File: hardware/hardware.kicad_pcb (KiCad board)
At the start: 2 copper layers, 45 x 45 mm, 27 parts, among them J2 USB_B_Micro, J3 Conn_01x05_Pin, U1 CH32V003F4P6, U3 AMS1117-3.3

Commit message: fix button
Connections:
- U1 pad 16: unconnected-(U1-PC6/MOSI-Pad16) -> BUTTON
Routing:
- net BUTTON: track 114.3 -> 134.1 mm, vias 0 -> 2

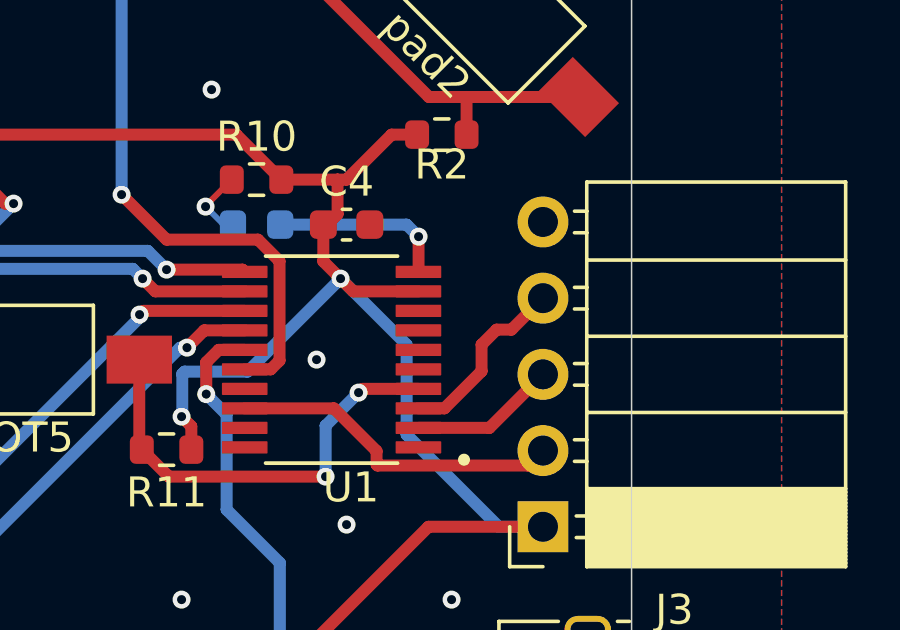
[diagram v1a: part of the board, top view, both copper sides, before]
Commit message: fix mcu ground issue
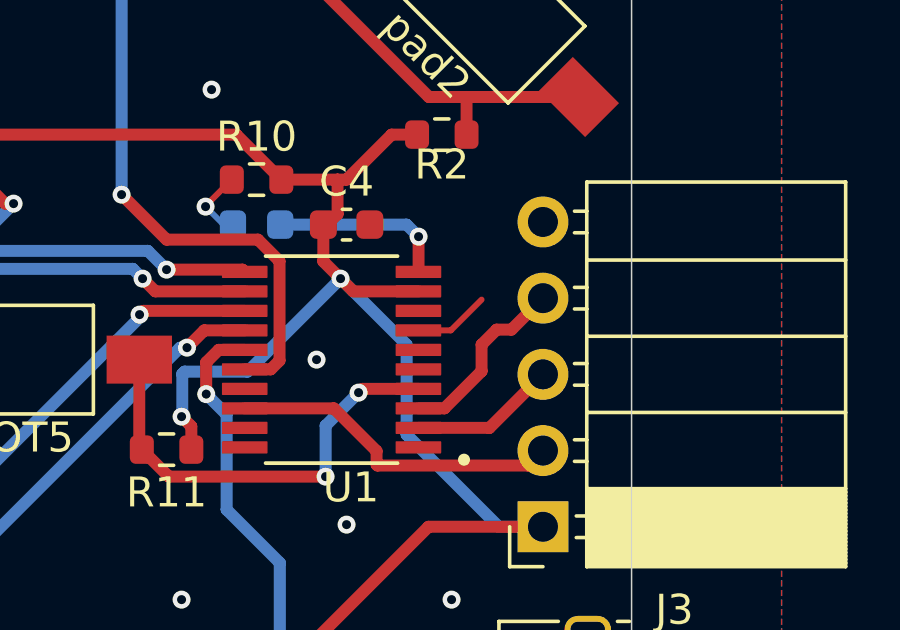
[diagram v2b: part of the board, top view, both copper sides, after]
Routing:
- net GND: track 2.62 -> 5.15 mm
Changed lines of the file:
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@@
 		(at 120 67 180)
 		(property "Reference" "U1"
-			(at -0.645 -4.262 360)
+			(at -0.645 -4.262 0)
 			(layer "F.SilkS")
 			(effects
@@
 		)
 		(property "Value" "CH32V003F4P6"
-			(at 6.975 4.262 360)
+			(at 6.975 4.262 0)
 			(layer "F.Fab")
 			(effects
@@
 		)
 		(property "Footprint" "CH32V003F4P6:SOP65P640X121-20N"
-			(at 0 0 360)
+			(at 0 0 0)
 			(layer "F.Fab")
 			(hide yes)
@@
 		)
 		(property "Datasheet" ""
-			(at 0 0 360)
+			(at 0 0 0)
 			(layer "F.Fab")
 			(hide yes)
@@
 		)
 		(property "Description" ""
-			(at 0 0 360)
+			(at 0 0 0)
 			(layer "F.Fab")
 			(hide yes)
@@
 		(tags "SPST button tactile switch")
 		(property "Reference" "BOOT5"
-			(at 0 -2.6 360)
+			(at 0 -2.6 0)
 			(layer "F.SilkS")
 			(effects
@@
 		)
 		(property "Value" "SW_Push"
-			(at 0 3 360)
+			(at 0 3 0)
 			(layer "F.Fab")
 			(effects
@@
 		)
 		(fp_text user "${REFERENCE}"
-			(at 0 -2.6 360)
+			(at 0 -2.6 0)
 			(layer "F.Fab")
 			(effects
@@
 		(tags "resistor")
 		(property "Reference" "R5"
-			(at 0 -1.43 360)
+			(at 0 -1.43 0)
 			(layer "F.SilkS")
 			(effects
@@
 		)
 		(property "Value" "R_Small"
-			(at 0 1.43 360)
+			(at 0 1.43 0)
 			(layer "F.Fab")
 			(effects
@@
 		)
 		(fp_text user "${REFERENCE}"
-			(at 0 0 360)
+			(at 0 0 0)
 			(layer "F.Fab")
 			(effects
@@
 		(tags "resistor")
 		(property "Reference" "R7"
-			(at 0 -1.43 360)
+			(at 0 -1.43 0)
 			(layer "F.SilkS")
 			(effects
@@
 		)
 		(property "Value" "R_Small"
-			(at 0 1.43 360)
+			(at 0 1.43 0)
 			(layer "F.Fab")
 			(effects
@@
 		)
 		(fp_text user "${REFERENCE}"
-			(at 0 0 360)
+			(at 0 0 0)
 			(layer "F.Fab")
 			(effects
@@
 		(tags "resistor")
 		(property "Reference" "R11"
-			(at 0 -1.43 360)
+			(at 0 -1.43 0)
 			(layer "F.SilkS")
 			(effects
@@
 		)
 		(property "Value" "R_Small"
-			(at 0 1.43 360)
+			(at 0 1.43 0)
 			(layer "F.Fab")
 			(effects
@@
 		)
 		(fp_text user "${REFERENCE}"
-			(at 0 0 360)
+			(at 0 0 0)
 			(layer "F.Fab")
 			(effects
@@
 		(tags "Through hole angled socket strip THT 1x05 2.54mm single row")
 		(property "Reference" "J3"
-			(at -4.38 -2.77 360)
+			(at -4.38 -2.77 0)
 			(layer "F.SilkS")
 			(effects
@@
 		)
 		(property "Value" "Conn_01x05_Pin"
-			(at -4.38 12.93 360)
+			(at -4.38 12.93 0)
 			(layer "F.Fab")
 			(effects
@@
 		(tags "resistor")
 		(property "Reference" "R9"
-			(at 0 1.5 360)
+			(at 0 1.5 0)
 			(layer "F.SilkS")
 			(effects
@@
 		)
 		(property "Value" "R_Small"
-			(at 0 1.43 360)
+			(at 0 1.43 0)
 			(layer "F.Fab")
 			(effects
@@
 		)
 		(fp_text user "${REFERENCE}"
-			(at 0 0 360)
+			(at 0 0 0)
 			(layer "F.Fab")
 			(effects
@@
 	)
 	(segment
+		(start 122.895 66.025)
+		(end 123.975 66.025)
+		(width 0.2)
+		(layer "F.Cu")
+		(net 1)
+	)
+	(segment
 		(start 124.185996 78.185996)
 		(end 123.5 77.5)
@@
 		(layer "F.Cu")
 		(net 1)
+	)
+	(segment
+		(start 123.975 66.025)
+		(end 125 65)
+		(width 0.2)
+		(layer "F.Cu")
+		(net 1)
